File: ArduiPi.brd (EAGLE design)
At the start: 85 x 56 mm, 59 parts, among them IC1 DS2482-100S, IC2 AVR-MEGA8-PPTH, J1 VIN, J3 ISP, Q1 BS170, Q2 BS170, Q3 BS170, Q4 BS170, U1 LD1117 3V3, U2 78M05, U3 TXB0108, U4 TXB0108, Y1 16MHz

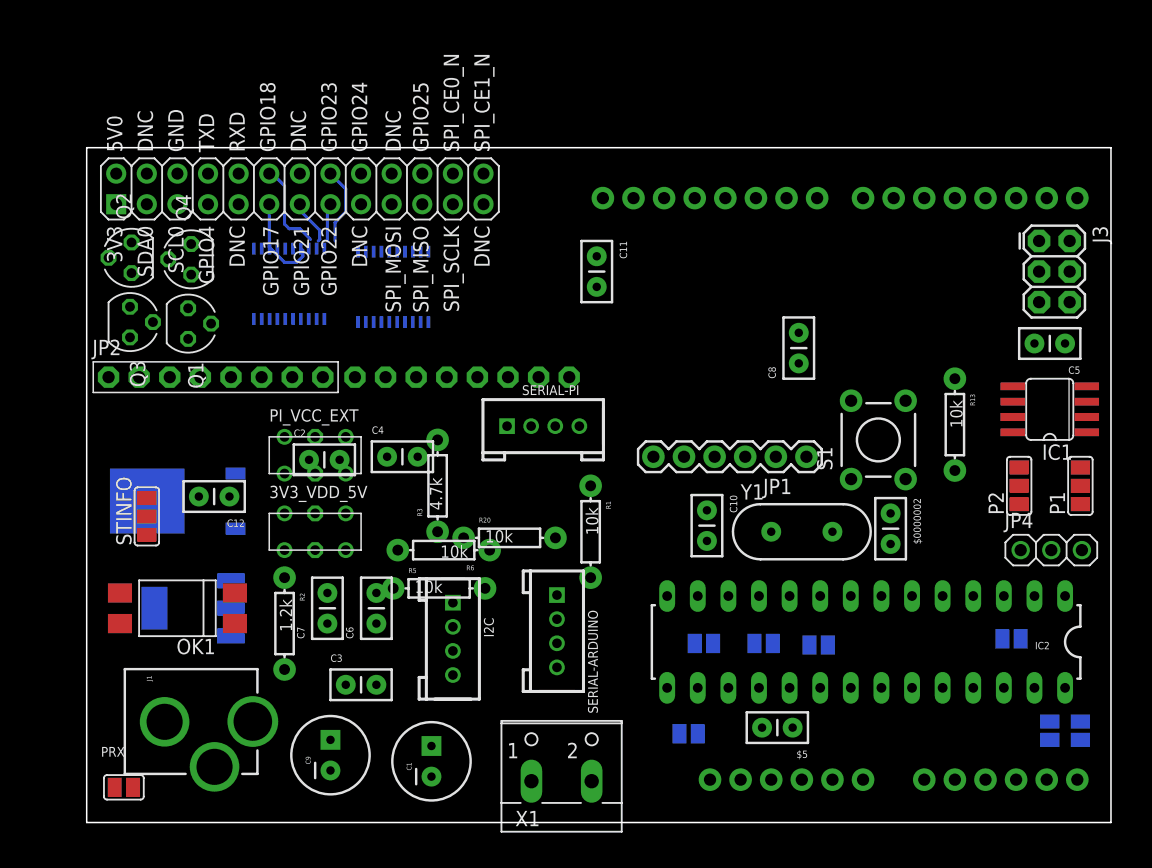
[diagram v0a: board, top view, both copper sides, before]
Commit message: Reordered Componnents on PCB for bettre view
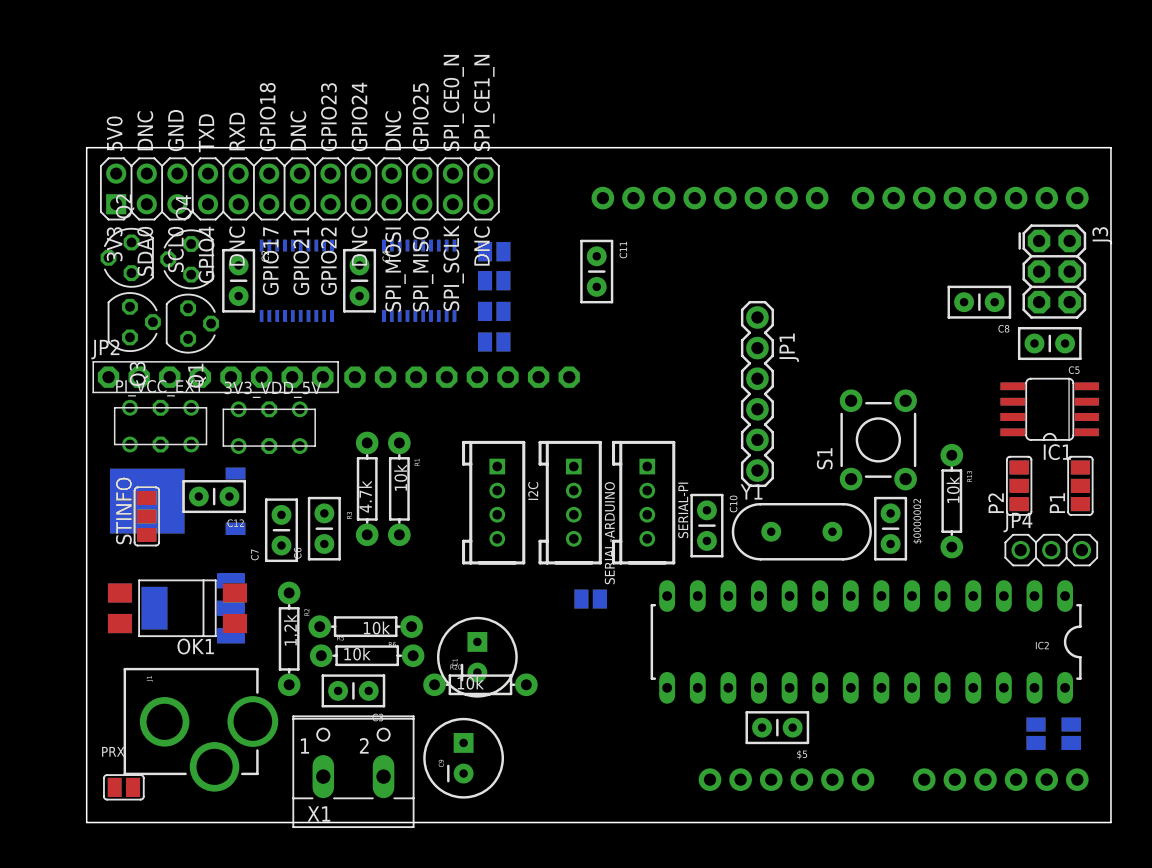
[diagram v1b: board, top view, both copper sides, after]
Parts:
- moved PCLK 38.6 mm to (33.9, 42.4)
- moved PMISO 37.5 mm to (33.9, 45.0), turned to 180 degrees
- moved PMOSI 36.9 mm to (33.9, 47.4)
- moved PSS 36.3 mm to (33.9, 39.9)
- moved PTX 35.1 mm to (41.9, 18.5), turned to 180 degrees
- moved X1 17.3 mm to (22.2, 5.08)
- moved C2 17.2 mm to (12.7, 46.2), turned to 270 degrees
- moved C8 17.0 mm to (75.4, 43.2), turned to 180 degrees
- moved R1 16.3 mm to (26.0, 27.7)
- moved C4 16.0 mm to (22.7, 46.2), turned to 270 degrees
- moved PI_VCC_EXT 13.1 mm to (6.22, 32.9)
- moved R20 12.4 mm to (32.8, 11.4)
- moved JP1 12.3 mm to (55.8, 41.9), turned to 270 degrees
- moved I2C 11.9 mm to (34.2, 26.5)
- moved C9 11.1 mm to (31.4, 5.33)
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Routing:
- net GPIO17: track 7.59 -> 0.00 mm
- net GPIO18: track 7.55 -> 0.00 mm
- net N$15: track 5.94 -> 0.00 mm
- net N$13: track 3.60 -> 0.00 mm
- net N$14: track 2.57 -> 0.00 mm

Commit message: Final Design
Final Design
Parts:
- removed $0000002: 22pF, SparkFun:CAP-PTH-SMALL2
- removed $5: 0.1uF, SparkFun:CAP-PTH-SMALL2
- removed JP3: PI I/O, adafruit:1X08-BIG
- removed JP4: 1-Wire, adafruit:1X03
- removed P1, P2: (no value), Seeedstudio-Discreter.rpt:3P-SMD-2X4.8
- removed R13, R20: 10k, SparkFun:AXIAL-0.3
- removed RASPBERRY: RASPBERRYPI_BB, microbuilder:RASBERRYPI_SHIELD
- removed S1: RESET, SparkFun:TACTILE-PTH
- removed SERIAL-ARDUINO, SERIAL-PI: GROVE, Connector:4P-LEADED-2.0
- removed Y1: 16MHz, SparkFun:HC49US
- added ARDUINO-SERIAL, PI-SERIAL: GROVE, Connector:4P-LEADED-2.0
- added C13, C14, C15, C16: 0.1uF, resistor:C0603
- added D1: 1N4004, adafruit:DO41-10
- added I2C-OLED, PC1, POWER: DNP, Seeedstudio-Connector:6P-2.54
- added J10: ICSP, SparkFun:2X3
- added J11: DNP, Seeedstudio-Connector:4P-2.54-80/40MIL
- added J12, J13, PB1, PD1, SPI-OLED, SPI-OLED-PI: DNP, Seeedstudio-Connector:8P-2.54
- added J2, J4, J5, J6, J7, J8: DNP, Seeedstudio-Connector:3P-2.54
- added J9: DC-044-AH, For_Test_Albert:DC-404
- added K1: RESET, Seeedstudio-Discrete.rpt:2P-7.62X3.56-90D
- added LED1: BLUE, led:CHIP-LED0603
- added LED2: RED, led:CHIP-LED0603
- added PAD1: PAD1, Seeedstudio-Discreter.rpt:3P-SMD-2X3
- added PAD2: PAD0, Seeedstudio-Discreter.rpt:3P-SMD-2X3
- added PI-P1: PI-P1, pi:RASPBERRYPI_SHIELD
- added PLED1: PLED1, Seeedstudio-Discreter.rpt:3P-SMD-2X3
- added PLED2: PLED2, Seeedstudio-Discreter.rpt:3P-SMD-2X3
- added PSSPI: PSSPI, Seeedstudio-Discreter.rpt:3P-SMD-2X3
- added PVDD: PVDD, Seeedstudio-Discreter.rpt:2P-SMD-2X3.3
- added Q5: BSS84, transistor-small-signal:SOT23
- added R10: 180, resistor:R0805
- added R4: 4.7K, resistor:R0805
- added R7, R8: 10k, resistor:R0603
- added R9: 120, resistor:R0805
- added U5: TXB0108, adafruit:TSSOP20
- C1: value 47uF -> 0.1uF; device SparkFun:CPOL-RADIAL-100UF-25V -> Seeedstudio-Discrete.rpt:CERAMIC-1.4
- C10: value 22pF -> 0.1uF; device SparkFun:CAP-PTH-SMALL2 -> Seeedstudio-Discrete.rpt:CERAMIC-1.4
- C11, C12: device SparkFun:CAP-PTH-SMALL2 -> resistor:C0603
- C2, C3: value 0.1uF -> 22pF; device SparkFun:CAP-PTH-SMALL2 -> Seeedstudio-Discrete.rpt:CERAMIC-1.4
- C4, C5, C8: device SparkFun:CAP-PTH-SMALL2 -> Seeedstudio-Discrete.rpt:CERAMIC-1.4
- C6: value 0.1uF -> 47uF; device SparkFun:CAP-PTH-SMALL2 -> SparkFun:CPOL-RADIAL-10UF-25V
- C7: value 0.1uF -> 10uF; device SparkFun:CAP-PTH-SMALL2 -> SparkFun:CPOL-RADIAL-10UF-25V
- C9: value 10uF -> 0.1uF; device SparkFun:CPOL-RADIAL-100UF-25V -> resistor:C0603
- IC1: value DS2482-100S -> AVR-MEGA8-PPTH; device 1wire:SO08 -> SparkFun:DIL28-3
- IC2: value AVR-MEGA8-PPTH -> DS2482-100S; device SparkFun:DIL28-3 -> 1wire:SO08
- J1: value VIN -> Teleinfo; device SparkFun:POWER_JACK_PTH_LOCK -> Seeedstudio-Connector:2P-2.54
- J3: value ISP -> DNP; device SparkFun:2X3 -> Seeedstudio-Connector:3P-2.54
- JP2: value PI I/O -> 1-Wire; device adafruit:1X08-BIG -> adafruit:1X03
- PCLK: value (none) -> PCLK
- PMISO: value (none) -> PMISO
- PMOSI: value (none) -> PMOSI
- PRX: value (none) -> PRX
- PSCL: value (none) -> PSCL
- PSDA: value (none) -> PSDA
- PSS: value (none) -> PSS; device Seeedstudio-Discreter.rpt:2P-SMD-2X3.3 -> Seeedstudio-Discreter.rpt:3P-SMD-2X3
- PTX: value (none) -> PTX
- Q1, Q2, Q3, Q4: value BS170 -> BSS138; device transistor-small-signal:SOT54E -> Seeedstudio-Discreter.rpt:SOT23
- R1: value 10k -> 1.2k; device SparkFun:AXIAL-0.3 -> resistor:R0805
- R2: value 1.2k -> 10k; device SparkFun:AXIAL-0.3 -> resistor:R0805
- R3: device SparkFun:AXIAL-0.3 -> resistor:R0805
- R5: value 10k -> 4.7K; device SparkFun:AXIAL-0.3 -> resistor:R0805
- R6: device SparkFun:AXIAL-0.3 -> resistor:R0603
- STINFO: value (none) -> STINFO; device Seeedstudio-Discreter.rpt:3P-SMD-2X4.8 -> Seeedstudio-Discreter.rpt:3P-SMD-2X3
- U1: value LD1117 3V3 -> 78M05; device Seeedstudio-IC:SOT-223 -> SeedStudio-IC:TO252
- U2: value 78M05 -> LD1117 3V3; device SeedStudio-IC:TO252 -> Seeedstudio-IC:SOT-223
- U3: value TXB0108 -> TXB0104; device adafruit:TSSOP20 -> adafruit:TSSOP14
- X1: value (none) -> 16Mhz; device _c2h:W237-102 -> Seeedstudio-Discrete.rpt:HC49/S
- moved JP2 71.1 mm to (81.7, 43.1), turned to 270 degrees
- moved C8 66.5 mm to (21.0, 5.08), turned to 0 degrees
- moved C9 59.0 mm to (81.3, 36.8), turned to 180 degrees
- moved C2 58.5 mm to (66.7, 23.7)
- moved JP1 52.6 mm to (3.43, 37.0)
- moved C4 51.5 mm to (69.2, 24.0)
- moved J3 48.1 mm to (35.6, 27.9), turned to 0 degrees
- moved X1 42.1 mm to (59.8, 24.0)
- moved PMOSI 37.6 mm to (53.1, 15.0), turned to 270 degrees
- moved C5 37.6 mm to (44.3, 46.7)
- moved PCLK 37.1 mm to (58.9, 15.0), turned to 270 degrees
- moved PMISO 37.1 mm to (55.8, 15.0), turned to 270 degrees
- moved STINFO 36.7 mm to (35.7, 5.21), flipped to the bottom, turned to 0 degrees
- moved C11 35.0 mm to (7.62, 43.2), flipped to the bottom, turned to 180 degrees
- moved J1 34.9 mm to (34.3, 1.91)
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- renumbered SCL to PSCL, SDA to PSDA
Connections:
- new net GPIO28: PI-P1.P5.3, U3.2
- new net GPIO29: PI-P1.P5.4, U3.3
- new net GPIO30: PI-P1.P5.5, U3.4
- new net GPIO31: PI-P1.P5.6, U3.5
- new net IO28: J11.1, U3.13
- new net IO29: J11.2, U3.12
- new net IO30: J11.3, U3.11
- new net IO31: J11.4, U3.10
- new net N$14: J1.2, R1.2
- new net N$15: IC2.6, Q5.1
- new net N$16: PLED1.2, R9.1
- new net N$17: LED1.A, R9.2
- new net N$18: LED2.A, R10.2
- new net N$19: R6.1, U3.8
- new net N$20: PLED2.2, R10.1
- new net SSPI: PSSPI.2, SPI-OLED-PI.8
- net 3V3: now also POWER.5
- net 3V3-EXT: now also C10.2, U2.2, U2.TER; no longer C7.1, U1.TER
- net 3V3-PI: now also C11.1, C12.1, C13.1, PI-P1.1, PI-P1.P5.2, Q3.1, Q4.1, R6.2, R7.2, R8.2, U3.1, U5.2; no longer C2.1, C3.1, Q2.G, Q4.G, R5.P$2, R6.P$2, RASPBERRY.1, U3.2
- net 5V-EXT: now also C7.1, C8.2, PLED2.1, PVDD.2, U1.2, U2.3; no longer C12.1, C9.1, U1.3, U2.2
- net 5V-PI: now also PI-P1.2, PI-P1.P5.1, PLED2.3; no longer RASPBERRY.2
- net AD0: now also IC1.23, PC1.1; no longer IC2.23
- net AD1: now also IC1.24, PC1.2; no longer IC2.24
- net AD2: now also IC1.25, PC1.3; no longer IC2.25
- net AD3: now also IC1.26, PC1.4; no longer IC2.26
- net AD4/SDA: now also IC1.27, PC1.5; no longer IC2.27
- net AD5/SCL: now also IC1.28, PC1.6; no longer IC2.28
- net AREF: now also C5.2, PB1.8; no longer C11.1
- net CE0: now also J13.6, PSS.3, PSSPI.3, U5.14; no longer JP3.6, PSS.1, U4.14
- net CE1: now also J13.7, PSS.1, PSSPI.1, U5.13; no longer JP3.7, U4.13
- net CE3: now also J13.8, U5.12; no longer JP3.8, U4.12
- net D0/RX-I: now also ARDUINO-SERIAL.1, IC1.2, PD1.1; no longer IC2.2
- net D1/TX-O: now also ARDUINO-SERIAL.2, IC1.3, PD1.2; no longer IC2.3
- net D10/SS: now also IC1.16, J6.3, PB1.3, SPI-OLED.8; no longer IC2.16
- net D11/MOSI: now also IC1.17, J10.4, J7.3, PB1.4, SPI-OLED.4; no longer IC2.17, J3.4
- net D12/MISO: now also IC1.18, J10.1, PB1.5; no longer IC2.18, J3.1
- net D13/SCK: now also IC1.19, J10.3, PB1.6, PLED1.1, SPI-OLED.5; no longer IC2.19, J3.3
- net D2: now also IC1.4, PD1.3, PLED1.3; no longer IC2.4
- net D3: now also IC1.5, J2.3, PD1.4; no longer IC2.5
- net D4: now also I2C-OLED.4, IC1.6, PD1.5; no longer IC2.6
- net D5: now also IC1.11, J3.3, PD1.6; no longer IC2.11
- net D6: now also IC1.12, J4.3, PD1.7; no longer IC2.12
- net D7: now also IC1.13, PD1.8, SPI-OLED.7; no longer IC2.13
- net D8: now also IC1.14, PB1.1, SPI-OLED.6; no longer IC2.14
- net D9: now also IC1.15, J5.3, PB1.2; no longer IC2.15
- net DTR: now also C1.2; no longer C8.1
- net GND: now also ARDUINO-SERIAL.4, C13.2, C14.2, C15.2, C16.2, C6.2, C8.1, I2C-OLED.3, IC1.22, IC1.8, IC2.3, J10.6, J2.2, J3.2, J4.2, J5.2, J6.2, J7.2, J8.2, J9.-, J9.CDN, JP2.3, K1.P$1, LED1.C, LED2.C, PAD1.1, PAD2.1, PB1.7, PI-P1.6, PI-P1.P5.7, PI-P1.P5.8, PI-SERIAL.4, POWER.2, POWER.3, SPI-OLED-PI.1, SPI-OLED.1, U1.3, U2.1, U3.7, U5.11; no longer $0000002.1, $5.1, C1.2, C6.1, IC1.3, IC2.22, IC2.8, J1.GND, J1.GNDBREAK, J3.6, P1.1, P2.1, RASPBERRY.6, S1.1, S1.2, SERIAL-ARDUINO.4, SERIAL-PI.4, U1.1, U2.3, U3.11
- net GPIO17: now also PI-P1.11, U4.3; no longer RASPBERRY.11, U3.3
- net GPIO18: now also PI-P1.12, U4.4; no longer RASPBERRY.12, U3.4
- net GPIO21: now also PI-P1.13, U4.5; no longer RASPBERRY.13, U3.5
- net GPIO22: now also PI-P1.15, U4.6; no longer RASPBERRY.15, U3.6
- net GPIO23: now also PI-P1.16, U4.7; no longer RASPBERRY.16, U3.7
- net GPIO24: now also PI-P1.18, U4.8; no longer RASPBERRY.18, U3.8
- net GPIO25: now also PI-P1.22, U4.9; no longer RASPBERRY.22, U3.9
- net GPIO4: now also PI-P1.7, U4.1; no longer RASPBERRY.7, U3.1
- net IO17: now also J12.2, U4.18; no longer JP2.2, U3.18
- net IO18: now also J12.3, J8.3, U4.17; no longer JP2.3, U3.17
- net IO21: now also J12.4, U4.16; no longer JP2.4, U3.16
- net IO22: now also J12.5, U4.15; no longer JP2.5, U3.15
- net IO23: now also J12.6, U4.14; no longer JP2.6, U3.14
- net IO24: now also J12.7, SPI-OLED-PI.6, U4.13; no longer JP2.7, U3.13
- net IO25: now also J12.8, SPI-OLED-PI.7, U4.12; no longer JP2.8, U3.12
- net IO4: now also J12.1, U4.20; no longer JP2.1, U3.20
- net MISO: now also J13.4, U5.16; no longer JP3.4, U4.16
- net MISO-PI: now also PI-P1.21, U5.5; no longer RASPBERRY.21
- net MOSI: now also J13.3, SPI-OLED-PI.4, U5.17; no longer JP3.3, U4.17
- net MOSI-PI: now also PI-P1.19, U5.4; no longer RASPBERRY.19
- net N$1: now also R3.1; no longer R3.P$1
- net N$10: now also JP1.VCC, PVDD.1; no longer R2.P$2, X1.1
- net N$11: now also IC2.7, PAD1.2; no longer IC1.7, P1.2
- net N$12: now also D1.A, J9.+; no longer U1.2
- net N$13: now also R8.1, U5.10; no longer R6.P$1, U4.10
- net N$2: now also IC2.8, PAD2.2; no longer IC1.8, P2.2
- net N$3: now also C3.1, IC1.10, X1.1; no longer $0000002.2, IC2.9, Y1.2
- net N$4: now also C2.1, IC1.9, X1.2; no longer C10.2, IC2.10, Y1.1
- net N$5: now also Q1.3, Q3.3; no longer Q2.D, Q3.D
- net N$6: now also Q2.3, Q4.3; no longer Q1.D, Q4.D
- net N$7: now also R7.1, U4.10; no longer R5.P$1, U3.10
- net N$8: now also R1.1; no longer R2.P$1
- net N$9: now also J1.1; no longer X1.2
- net OW: now also IC2.2, JP2.2, Q5.3; no longer IC1.2, JP4.2
- net RESET: now also C1.1, IC1.1, J10.5, K1.P$2, POWER.6, R2.2; no longer C8.2, IC2.1, J3.5, R13.P$1, S1.3, S1.4
- net RXD: now also J13.2, PI-SERIAL.1, U5.18; no longer JP3.2, U4.18
- net RXD-PI: now also PI-P1.10, U5.3; no longer RASPBERRY.10
- net SCL: now also I2C-OLED.5, IC2.4, Q2.2, R5.1; no longer IC1.4, Q1.S, R20.P$2
- net SCL-PI: now also PI-P1.5, Q4.2; no longer Q4.S, RASPBERRY.5
- net SCLK: now also J13.5, SPI-OLED-PI.5, U5.15; no longer JP3.5, U4.15
- net SCLK-PI: now also PI-P1.23, U5.6; no longer RASPBERRY.23
- net SDA: now also I2C-OLED.6, IC2.5, Q1.2, R4.1; no longer IC1.5, Q3.S, R1.P$1
- net SDA-PI: now also PI-P1.3, Q3.2; no longer Q2.S, RASPBERRY.3
- net SPI_CE0: now also PI-P1.24, U5.7; no longer RASPBERRY.24
- net SPI_CE1: now also PI-P1.26, U5.8; no longer RASPBERRY.26
- net TXD: now also J13.1, PI-SERIAL.2, U5.20; no longer JP3.1, U4.20
- net TXD-PI: now also PI-P1.8, U5.1; no longer RASPBERRY.8
- net VDD: now also ARDUINO-SERIAL.3, C14.1, C15.1, C16.1, C9.1, I2C-OLED.1, IC1.20, IC1.7, IC2.1, J10.2, J2.1, J3.1, J4.1, J5.1, J6.1, J7.1, J8.1, JP2.1, PAD1.3, PAD2.3, PI-SERIAL.3, POWER.4, Q1.1, Q2.1, Q5.2, R2.1, R3.2, R4.2, R5.2, SPI-OLED-PI.3, SPI-OLED.3, U3.14, U5.19; no longer $5.2, C5.2, C6.2, IC1.1, IC2.20, IC2.7, J3.2, JP4.1, P1.3, P2.3, Q1.G, Q3.G, R1.P$2, R13.P$2, R20.P$1, R3.P$2, SERIAL-ARDUINO.3, SERIAL-PI.3, U3.19
- net VIN: now also C6.1, D1.C, POWER.1, U1.1; no longer C1.1, J1.PWR, U2.1

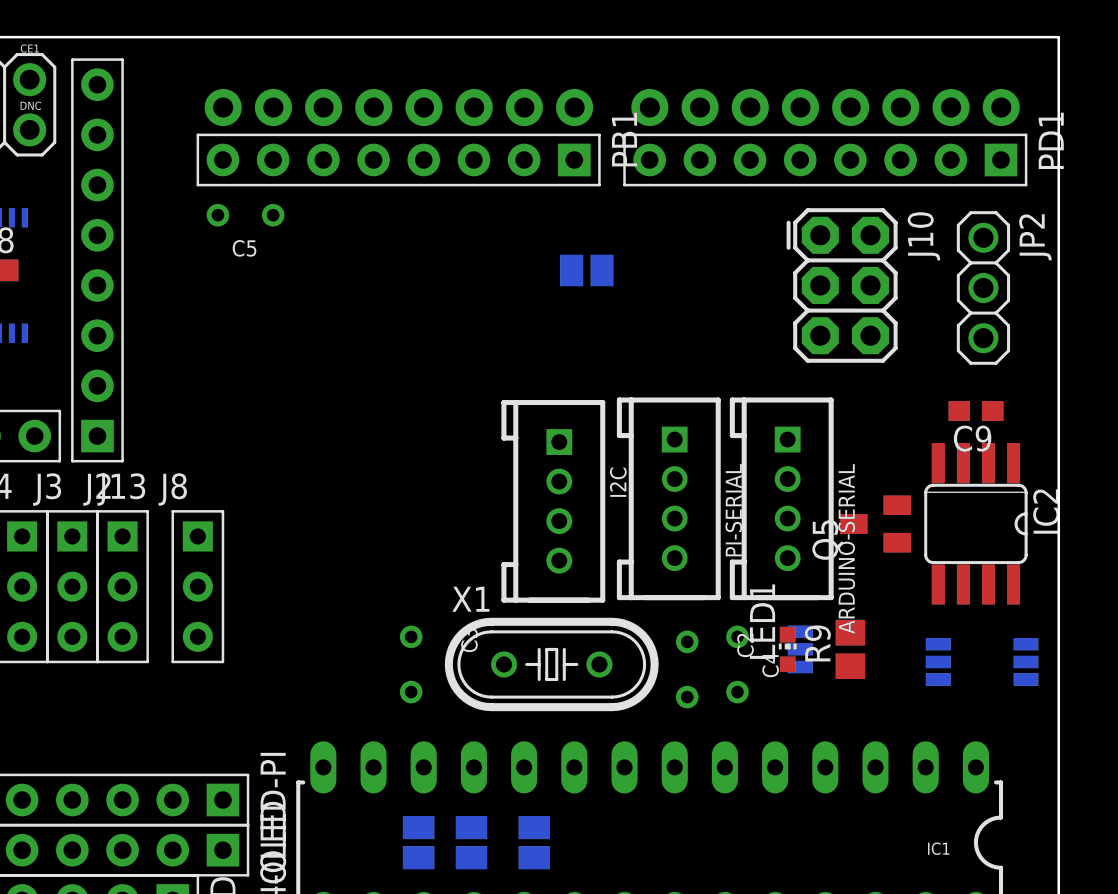
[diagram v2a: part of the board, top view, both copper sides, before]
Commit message: Added Pads
Added pads for One Wire and Prototyping area
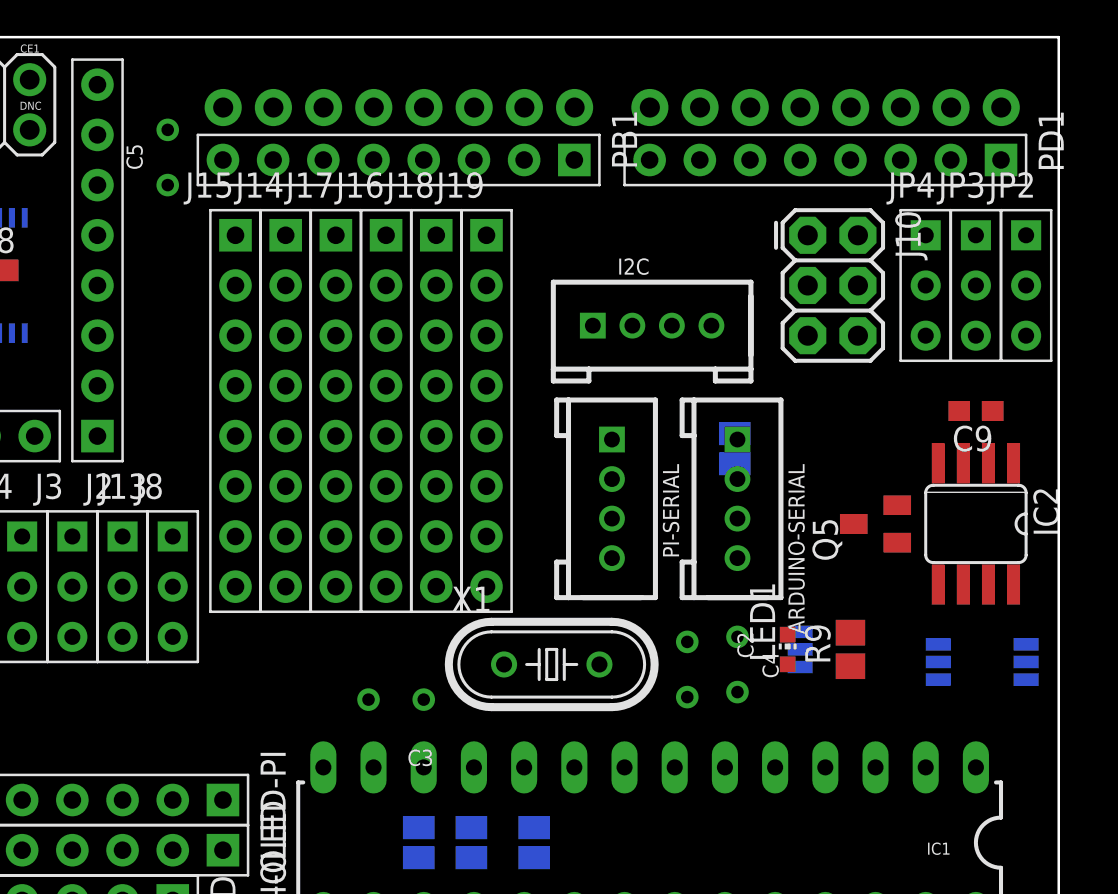
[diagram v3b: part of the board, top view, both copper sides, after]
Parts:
- added J14, J15, J16, J17, J18, J19: DNP, Seeedstudio-Connector:8P-2.54
- added JP3, JP4: DNP, Seeedstudio-Connector:3P-2.54
- JP2: value 1-Wire -> DNP; device adafruit:1X03 -> Seeedstudio-Connector:3P-2.54
- moved PTX 11.7 mm to (69.1, 34.9), turned to 90 degrees
- moved I2C 10.1 mm to (64.9, 41.1), turned to 0 degrees
- moved C5 4.90 mm to (40.4, 49.7), turned to 90 degrees
- moved PI-SERIAL 3.18 mm to (62.9, 32.4)
- moved ARDUINO-SERIAL 2.54 mm to (69.2, 32.4)
- moved JP2 2.16 mm to (83.8, 43.2), turned to 0 degrees
- moved C3 1.93 mm to (51.9, 22.2), turned to 180 degrees
- moved J8 1.27 mm to (40.6, 27.9)
- moved J10 0.64 mm to (72.8, 45.7)
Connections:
- net GND: now also J14.8, J15.8, J16.8, J17.8, J18.8, J19.8, JP3.3, JP4.3
- net OW: now also JP3.2, JP4.2
- net VDD: now also J14.1, J15.1, J16.1, J17.1, J18.1, J19.1, JP3.1, JP4.1

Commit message: Prototype Board
ArduiPi First Prototype Board
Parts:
- removed ARDUINO-HEADERS: ARDUINO_SHIELDNO_SILK, SparkFun-Boards:DUEMILANOVE_VIAS
- removed J10: ICSP, SparkFun:2X3
- removed J15, J16, J17, J18, J19: DNP, Seeedstudio-Connector:8P-2.54
- removed JP1: FTDI_BASICPTH, SparkFun-Connectors:FTDI_BASIC
- removed K1: RESET, Seeedstudio-Discrete.rpt:2P-7.62X3.56-90D
- added 24L01, 24L01-PI: DNP, Seeedstudio-Connector:2X4P-2.54
- added PINT: PINT, Discrete:2P-SMD-1.78X1.27
- added PINTPI: PINTPI, Discrete:2P-SMD-1.78X1.27
- added PPWM, PSS1: (no value), Discrete:3P-SMD-4.1X1.5
- added RESET: TS-118E, Discrete:4P-SMD-7X3.5X3.5H
- added U$3: (no value), Logo:LOGO_SILK
- added U$6: (no value), Logo:OSHW_FILLX200_NOTEXT
- added U6: (no value), For_Test_Albert_v6:ARDUINO
- C1, C10, C2, C3, C4, C5, C8: device Seeedstudio-Discrete.rpt:CERAMIC-1.4 -> Discrete:C0603
- C11, C12, C13, C14, C15, C16, C9: device resistor:C0603 -> Discrete:C0603
- C6: value 47uF -> 16V_47uF; device SparkFun:CPOL-RADIAL-10UF-25V -> Discrete:AVX-C
- C7: value 10uF -> 10V_10uF; device SparkFun:CPOL-RADIAL-10UF-25V -> Discrete:AVX-A
- D1: value 1N4004 -> M7; device adafruit:DO41-10 -> Discrete:D2010
- I2C-OLED, PC1, POWER: device Seeedstudio-Connector:6P-2.54 -> Connector:6P-2.54-65/35MIL
- J11: device Seeedstudio-Connector:4P-2.54-80/40MIL -> Connector:4P-65/35MIL
- J12, J13, PB1, PD1, SPI-OLED, SPI-OLED-PI: device Seeedstudio-Connector:8P-2.54 -> Connector:8P-2.54-65/35MIL
- J14: value DNP -> (none); device Seeedstudio-Connector:8P-2.54 -> Connector:6P-2.54-65/35MIL
- J9: device For_Test_Albert:DC-404 -> Connector:DC-044
- LED1, LED2: device led:CHIP-LED0603 -> Discrete:LED-0603
- PAD1: value PAD1 -> (none); device Seeedstudio-Discreter.rpt:3P-SMD-2X3 -> Discrete:3P-SMD-4.1X1.5
- PAD2: value PAD0 -> (none); device Seeedstudio-Discreter.rpt:3P-SMD-2X3 -> Discrete:3P-SMD-4.1X1.5
- PCLK, PMISO, PMOSI, PRX, PSCL, PSDA, PTX, PVDD: device Seeedstudio-Discreter.rpt:2P-SMD-2X3.3 -> Discrete:2P-SMD-1.78X1.27
- PLED1: value PLED1 -> (none); device Seeedstudio-Discreter.rpt:3P-SMD-2X3 -> Discrete:3P-SMD-4.1X1.5
- PLED2: value PLED2 -> (none); device Seeedstudio-Discreter.rpt:3P-SMD-2X3 -> Discrete:3P-SMD-4.1X1.5
- PSS: value PSS -> (none); device Seeedstudio-Discreter.rpt:3P-SMD-2X3 -> Discrete:3P-SMD-4.1X1.5
- PSSPI: value PSSPI -> (none); device Seeedstudio-Discreter.rpt:3P-SMD-2X3 -> Discrete:3P-SMD-4.1X1.5
- R1, R2, R3, R4, R5: device resistor:R0805 -> Discrete:R0603
- R10: value 180 -> 600; device resistor:R0805 -> Discrete:R0603
- R6, R7, R8: device resistor:R0603 -> Discrete:R0603
- R9: value 120 -> 360; device resistor:R0805 -> Discrete:R0603
- STINFO: value STINFO -> (none); device Seeedstudio-Discreter.rpt:3P-SMD-2X3 -> Discrete:3P-SMD-4.1X1.5
- X1: device Seeedstudio-Discrete.rpt:HC49/S -> Discrete:2P-SMD-5X3.2
- moved C5 58.3 mm to (82.7, 9.56), turned to 180 degrees
- moved STINFO 55.6 mm to (73.0, 46.4), turned to 180 degrees
- moved R9 55.2 mm to (21.0, 13.0), turned to 270 degrees
- moved LED1 53.9 mm to (21.0, 6.60), turned to 270 degrees
- moved PLED1 52.7 mm to (21.0, 13.4), turned to 0 degrees
- moved PC1 51.2 mm to (49.1, 49.8), turned to 270 degrees
- moved PRX 49.6 mm to (71.8, 41.9)
- moved PB1 48.4 mm to (74.5, 6.60), turned to 90 degrees
- moved PD1 48.3 mm to (51.6, 6.60), turned to 90 degrees
- moved J14 44.9 mm to (1.91, 30.5), turned to 180 degrees
- moved POWER 44.2 mm to (66.8, 49.8), turned to 90 degrees
- moved PSCL 42.1 mm to (57.8, 41.9), turned to 0 degrees
- moved PSDA 39.5 mm to (59.7, 41.9), turned to 0 degrees
- moved PVDD 32.9 mm to (4.83, 31.3), turned to 0 degrees
- moved PCLK 29.5 mm to (47.0, 41.9), turned to 0 degrees
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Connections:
- new net CSN: 24L01-PI.7, PSS1.MM
- new net IRQ: 24L01-PI.5, 24L01.5, PINT.2, PINTPI.2
- new net N$21: J2.1, J3.1, J4.1, J5.1, J6.1, J7.1, J8.1, PPWM.MM
- net 3V3: now also 24L01-PI.8, 24L01.8, U6.27; no longer ARDUINO-HEADERS.3.3V
- net 5V-EXT: now also C7.+, PLED2.00; no longer C7.1, PLED2.1
- net 5V-PI: now also PLED2.11; no longer PLED2.3
- net AD0: now also U6.17; no longer ARDUINO-HEADERS.A0
- net AD1: now also U6.18; no longer ARDUINO-HEADERS.A1
- net AD2: now also U6.19; no longer ARDUINO-HEADERS.A2
- net AD3: now also U6.20; no longer ARDUINO-HEADERS.A3
- net AD4/SDA: now also U6.21; no longer ARDUINO-HEADERS.A4
- net AD5/SCL: now also U6.22; no longer ARDUINO-HEADERS.A5
- net AREF: now also C5.1, U6.16; no longer ARDUINO-HEADERS.AREF, C5.2
- net CE0: now also PSS.11, PSS1.00, PSSPI.11; no longer PSS.3, PSSPI.3
- net CE1: now also PSS.00, PSS1.11, PSSPI.00; no longer PSS.1, PSSPI.1
- net D0/RX-I: now also J14.3, STINFO.00, U6.1; no longer ARDUINO-HEADERS.RX, JP1.TXO, STINFO.1
- net D1/TX-O: now also J14.2, U6.2; no longer ARDUINO-HEADERS.TX, JP1.RXI
- net D10/SS: now also PSS.MM, U6.11; no longer ARDUINO-HEADERS.D10, PSS.2, SPI-OLED.8
- net D11/MOSI: now also 24L01.6, U6.12, U6.32; no longer ARDUINO-HEADERS.D11, J10.4
- net D12/MISO: now also 24L01.4, U6.13, U6.36; no longer ARDUINO-HEADERS.D12, J10.1
- net D13/SCK: now also 24L01.3, PLED1.00, U6.14, U6.35; no longer ARDUINO-HEADERS.D13, J10.3, PLED1.1
- net D2: now also PINT.1, PLED1.11, U6.3; no longer ARDUINO-HEADERS.D2, PLED1.3
- net D3: now also 24L01.2, U6.4; no longer ARDUINO-HEADERS.D3
- net D4: now also 24L01.7, U6.5; no longer ARDUINO-HEADERS.D4
- net D5: now also U6.6; no longer ARDUINO-HEADERS.D5
- net D6: now also U6.7; no longer ARDUINO-HEADERS.D6
- net D7: now also U6.8; no longer ARDUINO-HEADERS.D7
- net D8: now also U6.9; no longer ARDUINO-HEADERS.D8
- net D9: now also SPI-OLED.8, U6.10; no longer ARDUINO-HEADERS.D9
- net DTR: now also J14.1; no longer JP1.DTR
- net GND: now also 24L01-PI.1, 24L01.1, C5.2, C6.-, C7.-, J14.5, J14.6, LED1.-, LED2.-, PAD1.00, PAD2.00, RESET.1, RESET.S1, RESET.S2, U6.15, U6.24, U6.25, U6.33; no longer ARDUINO-HEADERS.GND@0, ARDUINO-HEADERS.GND@1, ARDUINO-HEADERS.GND@2, C5.1, C6.2, C7.2, J10.6, J14.8, J15.8, J16.8, J17.8, J18.8, J19.8, JP1.CTS, JP1.GND, K1.P$1, LED1.C, LED2.C, PAD1.1, PAD2.1
- net IO22: now also 24L01-PI.2
- net IO23: now also PINTPI.1
- net MISO: now also 24L01-PI.4
- net MOSI: now also 24L01-PI.6
- net N$1: now also STINFO.MM; no longer STINFO.2
- net N$10: now also J14.4; no longer JP1.VCC
- net N$11: now also PAD1.MM; no longer PAD1.2
- net N$12: now also D1.+; no longer D1.A
- net N$16: now also PLED1.MM; no longer PLED1.2
- net N$17: now also LED1.+; no longer LED1.A
- net N$18: now also LED2.+; no longer LED2.A
- net N$2: now also PAD2.MM; no longer PAD2.2
- net N$20: now also PLED2.MM; no longer PLED2.2
- net RESET: now also RESET.2, U6.28, U6.34; no longer ARDUINO-HEADERS.RES, J10.5, K1.P$2
- net RXD: now also STINFO.11; no longer STINFO.3
- net SCLK: now also 24L01-PI.3
- net SSPI: now also PSSPI.MM; no longer PSSPI.2
- net VDD: now also PAD1.11, PAD2.11, PPWM.00, U6.26, U6.31; no longer ARDUINO-HEADERS.5V, J10.2, J14.1, J15.1, J16.1, J17.1, J18.1, J19.1, J2.1, J3.1, J4.1, J5.1, J6.1, J7.1, J8.1, PAD1.3, PAD2.3
- net VIN: now also C6.+, D1.-, PPWM.11, U6.23; no longer ARDUINO-HEADERS.VIN, C6.1, D1.C
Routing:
- net VDD: track 0.00 -> 333.0 mm, vias 0 -> 7
- net D13/SCK: track 0.00 -> 174.8 mm, vias 0 -> 2
- net SDA: track 0.00 -> 147.5 mm, vias 0 -> 7
- net D11/MOSI: track 0.00 -> 145.8 mm, vias 0 -> 3
- net D0/RX-I: track 0.00 -> 138.0 mm, vias 0 -> 2
- net SCL: track 0.00 -> 126.8 mm, vias 0 -> 5
- net D1/TX-O: track 0.00 -> 122.8 mm, vias 0 -> 1
- net D10/SS: track 0.00 -> 115.5 mm, vias 0 -> 4
- net VIN: track 0.00 -> 109.3 mm, vias 0 -> 6
- net RESET: track 0.00 -> 107.3 mm, vias 0 -> 4
- net D12/MISO: track 0.00 -> 101.9 mm, vias 0 -> 1
- net 3V3: track 0.00 -> 91.4 mm, vias 0 -> 2
- net D2: track 0.00 -> 91.2 mm, vias 0 -> 2
- net SCLK: track 0.00 -> 85.6 mm, vias 0 -> 1
- net N$1: track 0.00 -> 84.3 mm, vias 0 -> 3
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- added copper zone on layer 1, net 3V3-EXT
- added copper zone on layer 16, net 3V3-EXT
- added copper zone on layer 1, net GND
- added copper zone on layer 16, net GND
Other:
- board text added: "AJ1"
- board text added: "AJ2"
- board text added: "AJ3"
- board text added: "AJ4"
- board text added: "AJ5"
- board text added: "ArduiPi"
- board text added: "by Seeed Studio"
- board text added: "v0.9a 12/11/2012"
- board text added: "www.seeedstudio.com"
